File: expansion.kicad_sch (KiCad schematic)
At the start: 8 parts, among them J4 PMOD_A, J5 PMOD_B, J6 MEZZANINE

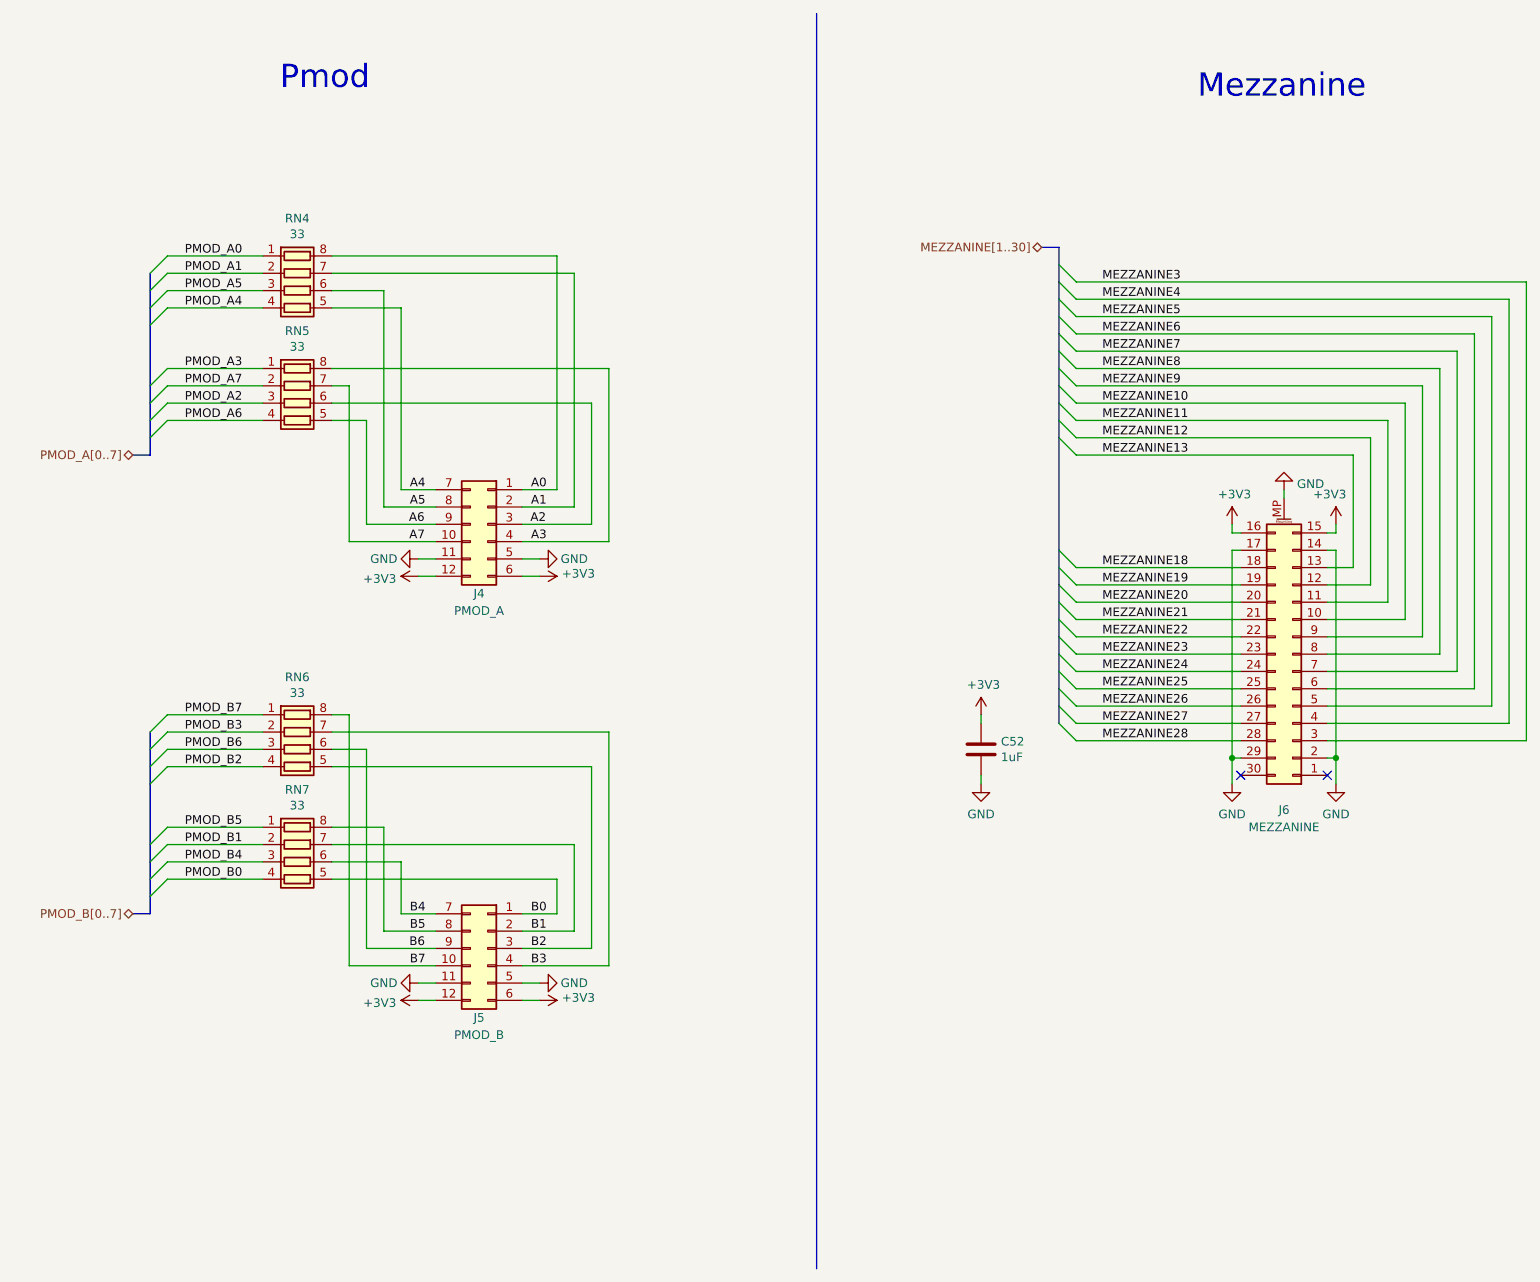
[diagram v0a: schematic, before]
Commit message: Add radio transceiver
Remove Cynthion-specific features
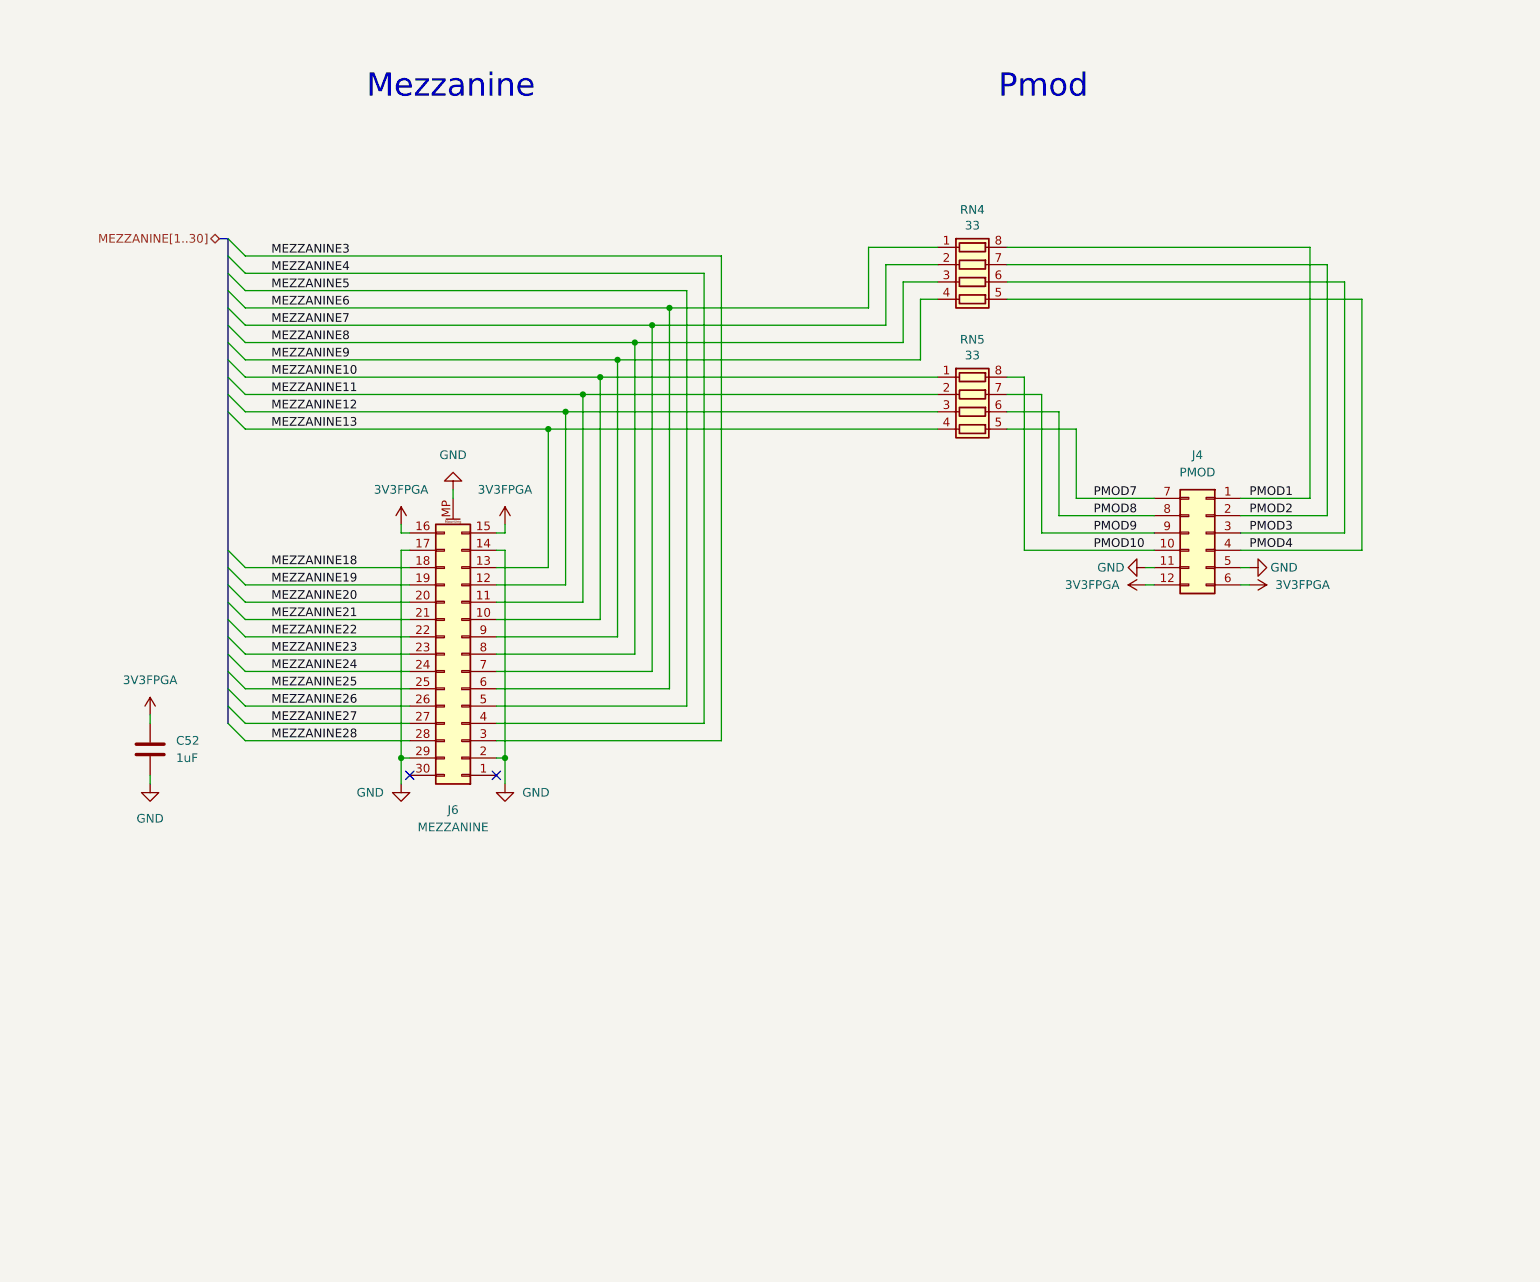
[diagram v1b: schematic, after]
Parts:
- removed J5: PMOD_B, mainboard:PinSocket_2x06_P2.54mm_PMOD, symbol Connector_Generic:Conn_02x06_Top_Bottom
- removed RN6, RN7: 33, Resistor_SMD:R_Array_Convex_4x0402, symbol Device:R_Pack04
- C52: Part Number CL05A105MQ5NNNC -> CL05A105KP5NNNC; Substitution CL05A105KQ5NNNC, CL05A105KP5NNNC, CL05A105KO5NNNC -> any equivalent
- J4: value PMOD_A -> PMOD; Note populate only when assembling for installation in enclosure -> (none)
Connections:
- net PMOD_A0 is gone; now on net MEZZANINE6: RN4.1 (R1.1)
- net PMOD_A1 is gone; now on net MEZZANINE7: RN4.2 (R2.1)
- net PMOD_A2 is gone; now on net MEZZANINE12: RN5.3 (R3.1)
- net PMOD_A3 is gone; now on net MEZZANINE10: RN5.1 (R1.1)
- net PMOD_A4 is gone; now on net MEZZANINE9: RN4.4 (R4.1)
- net PMOD_A5 is gone; now on net MEZZANINE8: RN4.3 (R3.1)
- net PMOD_A6 is gone; now on net MEZZANINE13: RN5.4 (R4.1)
- net PMOD_A7 is gone; now on net MEZZANINE11: RN5.2 (R2.1)
- net +3V3 renamed 3V3FPGA
- net A0 renamed PMOD1
- net A1 renamed PMOD2
- net A2 renamed PMOD3
- net PMOD3: now also RN4.6 (R3.2); no longer RN5.6 (R3.2)
- net A3 renamed PMOD10
- net PMOD10: now also J4.10 (Pin_10); no longer J4.4 (Pin_4)
- net A4 renamed PMOD4
- net PMOD4: now also J4.4 (Pin_4); no longer J4.7 (Pin_7)
- net A5 renamed PMOD8
- net PMOD8: now also RN5.6 (R3.2); no longer RN4.6 (R3.2)
- net A6 renamed PMOD7
- net PMOD7: now also J4.7 (Pin_7); no longer J4.9 (Pin_9)
- net A7 renamed PMOD9
- net PMOD9: now also J4.9 (Pin_9); no longer J4.10 (Pin_10)
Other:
- company: Copyright 2023 Great Scott Gadgets -> ${COPYRIGHT}
- title: URTI Mainboard -> ${TITLE}
- moved on the sheet: C52, J4, J6, RN4, RN5
